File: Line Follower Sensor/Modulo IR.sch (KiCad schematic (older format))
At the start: 10 parts, among them U1 LM358N, U10 100nF, U12 TCRT5000, U13 100R, U3 1K, U5 20K, U6 10K, U7 10k, U8 CON3_ET, U9 LED

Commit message: potenciometro cambiado
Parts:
- U7: footprint Potentiometers:Potentiometer_Trimmer-Suntan-TSR-3386P -> Potentiometers:Potentiometer_Trimmer_Bourns_3296W
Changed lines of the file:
@@
 EESchema Schematic File Version 2
 LIBS:Modulo IR-rescue
-LIBS:power
-LIBS:device
-LIBS:transistors
-LIBS:conn
-LIBS:linear
-LIBS:regul
-LIBS:74xx
-LIBS:cmos4000
-LIBS:adc-dac
-LIBS:memory
-LIBS:xilinx
-LIBS:microcontrollers
-LIBS:dsp
-LIBS:microchip
-LIBS:analog_switches
-LIBS:motorola
-LIBS:texas
-LIBS:intel
-LIBS:audio
-LIBS:interface
-LIBS:digital-audio
-LIBS:philips
-LIBS:display
-LIBS:cypress
-LIBS:siliconi
-LIBS:opto
-LIBS:atmel
-LIBS:contrib
-LIBS:valves
 LIBS:Modulo IR-cache
 EELAYER 25 0
@@
 F 0 "U7" H 6000 2700 50  0000 C CNN
 F 1 "10k" H 6000 2800 50  0000 C CNN
-F 2 "Potentiometers:Potentiometer_Trimmer-Suntan-TSR-3386P" H 6000 2800 50  0001 C CNN
+F 2 "Potentiometers:Potentiometer_Trimmer_Bourns_3296W" H 6000 2800 50  0001 C CNN
 F 3 "" H 6000 2800 50  0000 C CNN
 	1    6000 2800

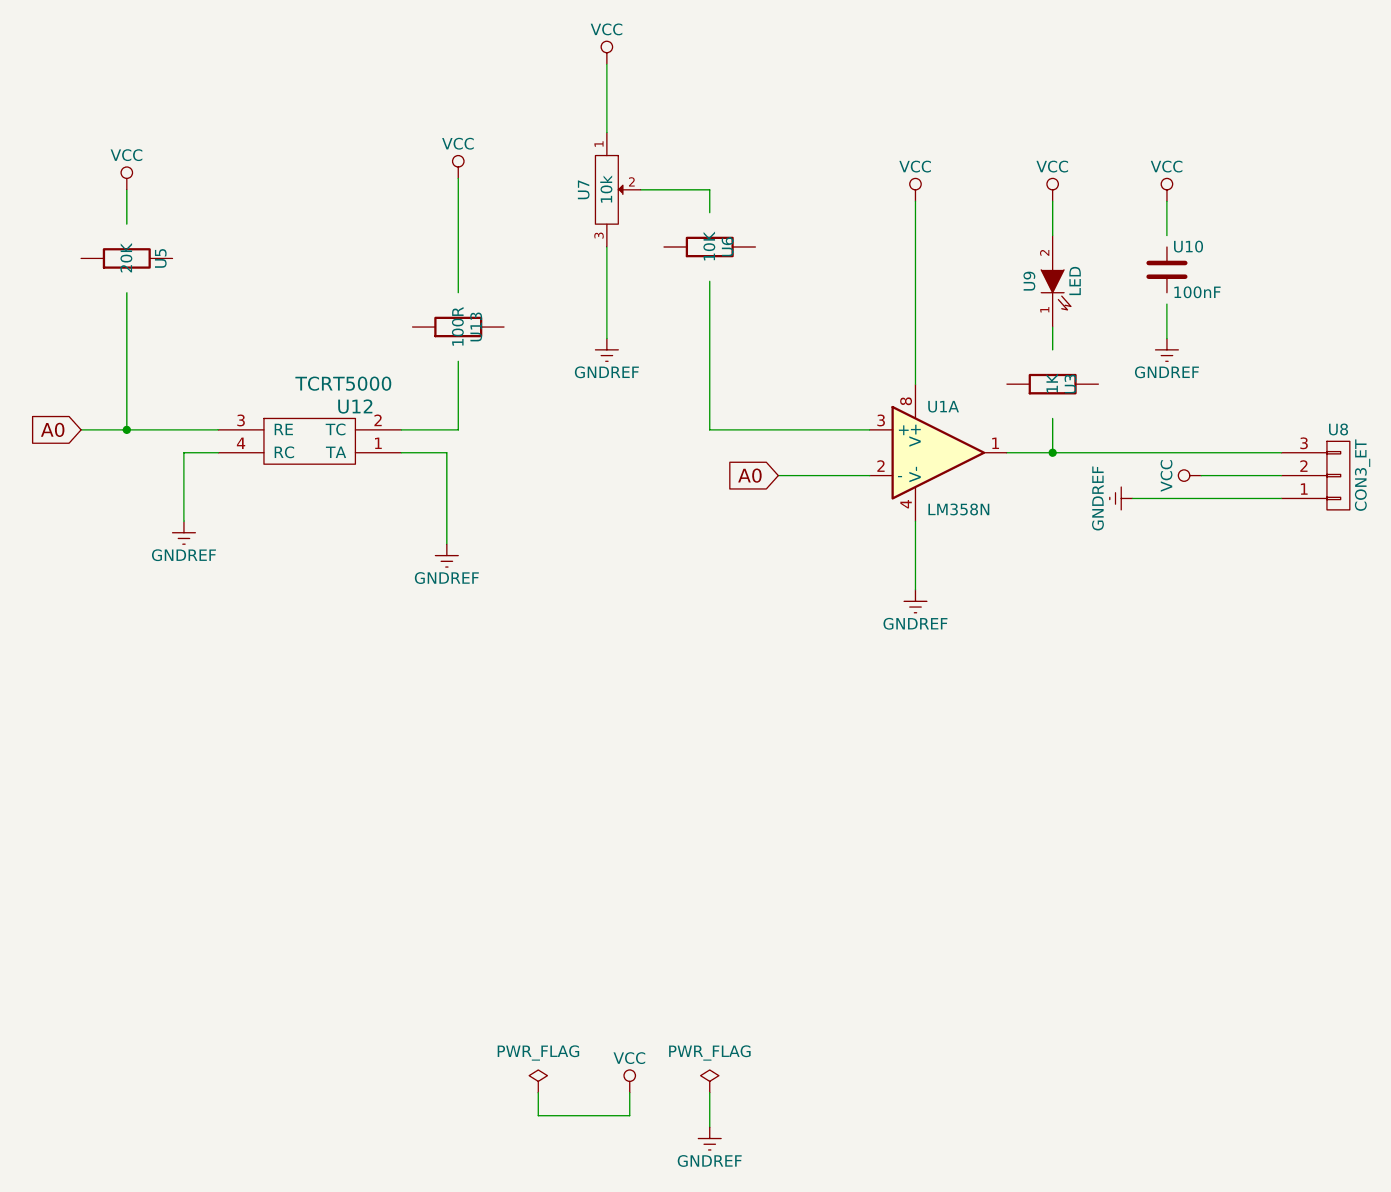
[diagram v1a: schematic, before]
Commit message: conector cambiado
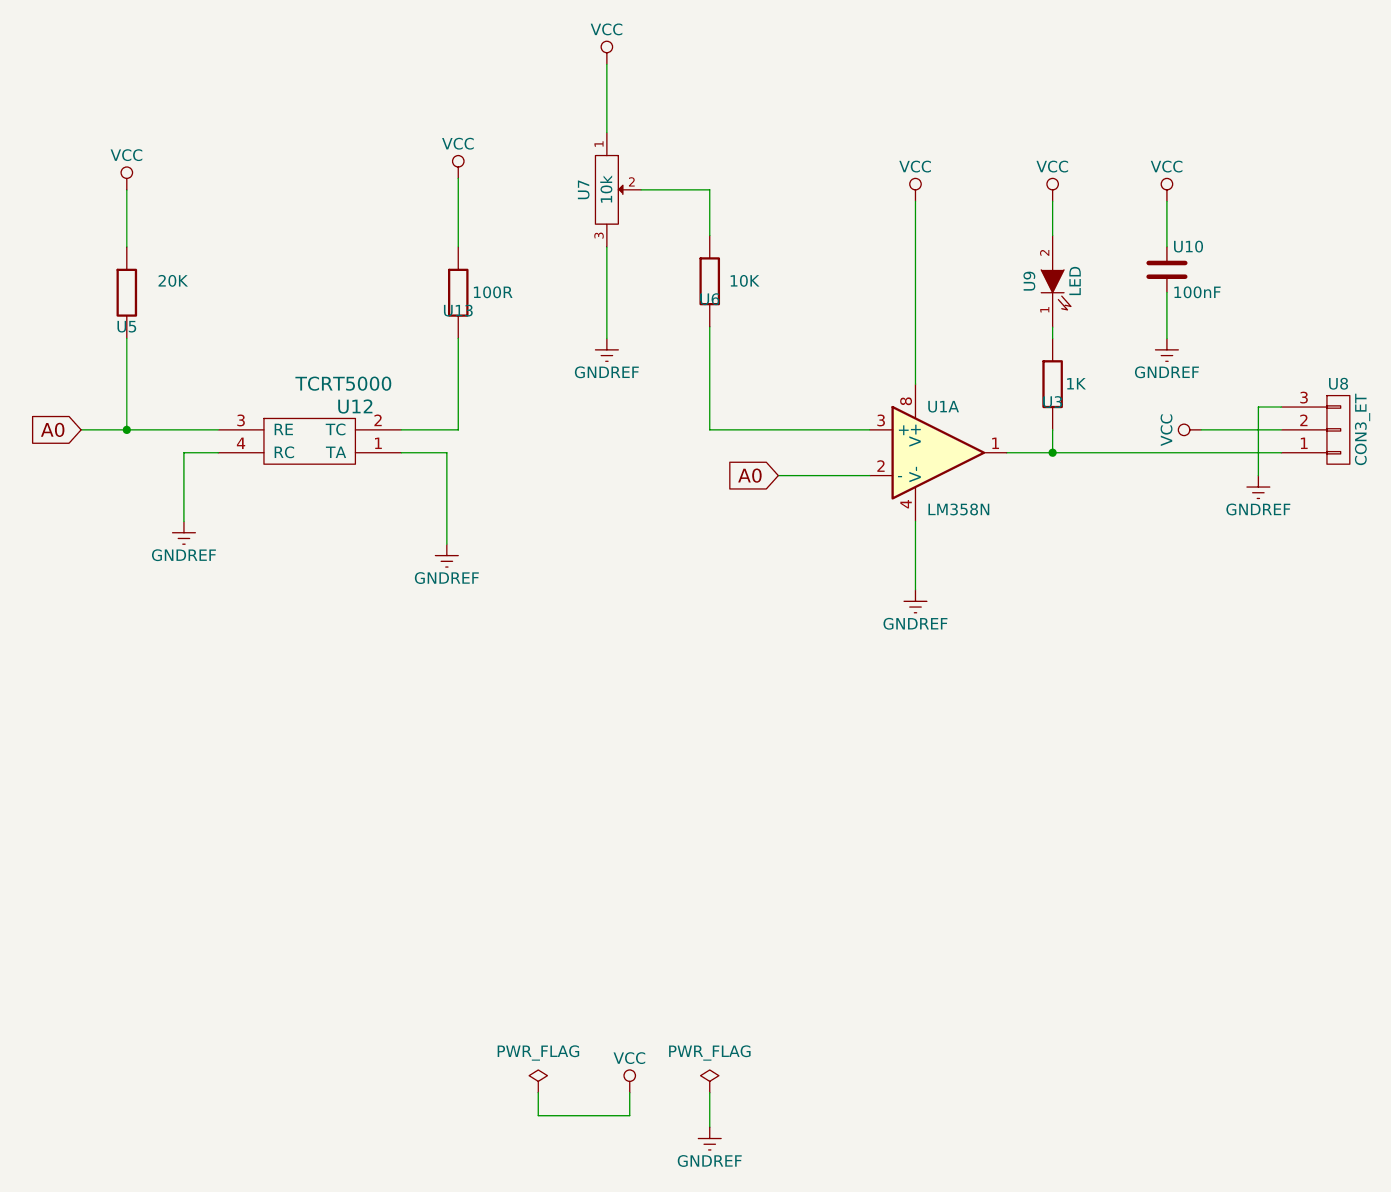
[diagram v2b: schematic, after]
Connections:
- wire segments 31 -> 32
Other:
- moved on the sheet: U13, U5, U6, U8
